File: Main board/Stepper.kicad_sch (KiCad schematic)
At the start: 10 parts, among them IC1 DRV8426RGER, J3 Conn_01x04

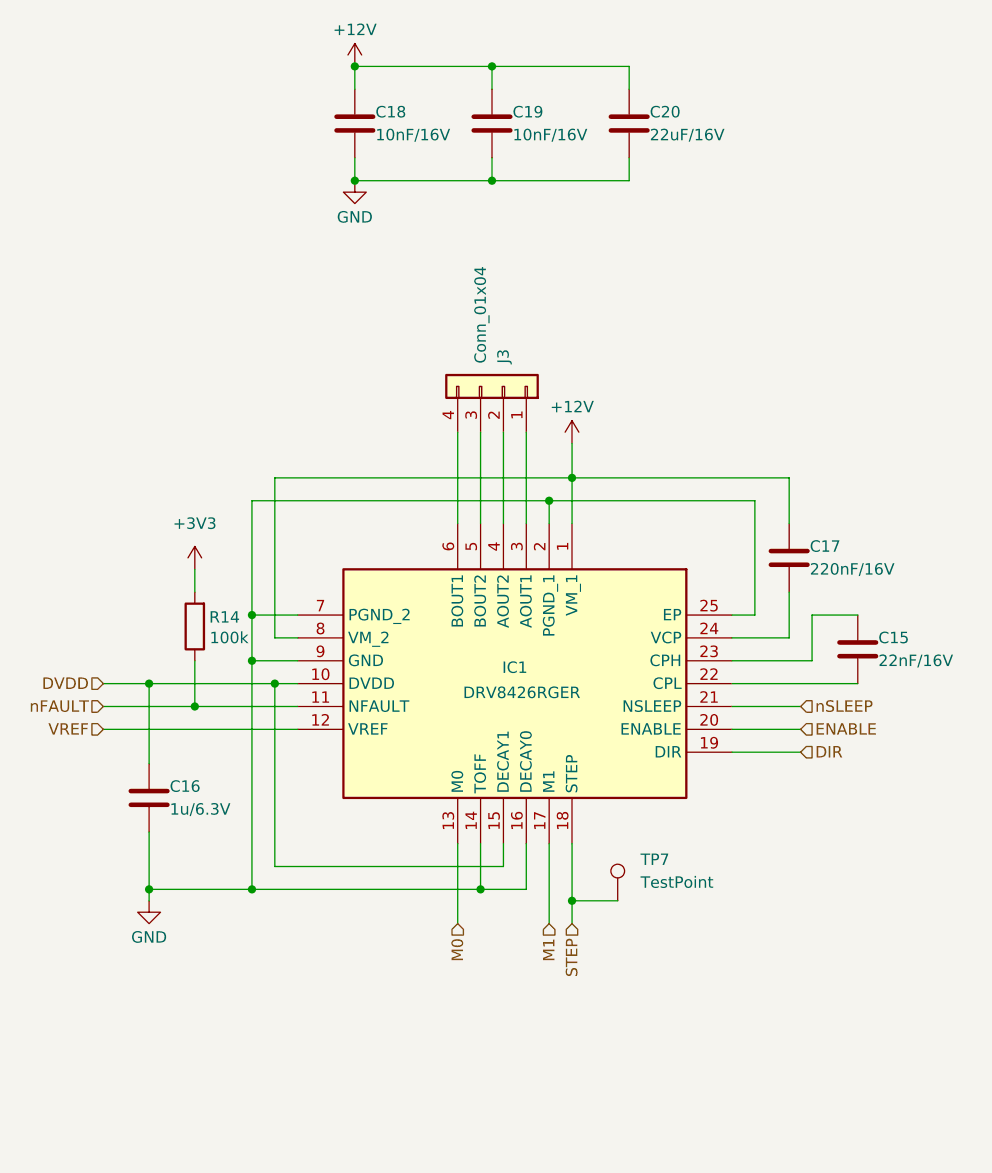
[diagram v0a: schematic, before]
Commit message: Main board updated to v0.3
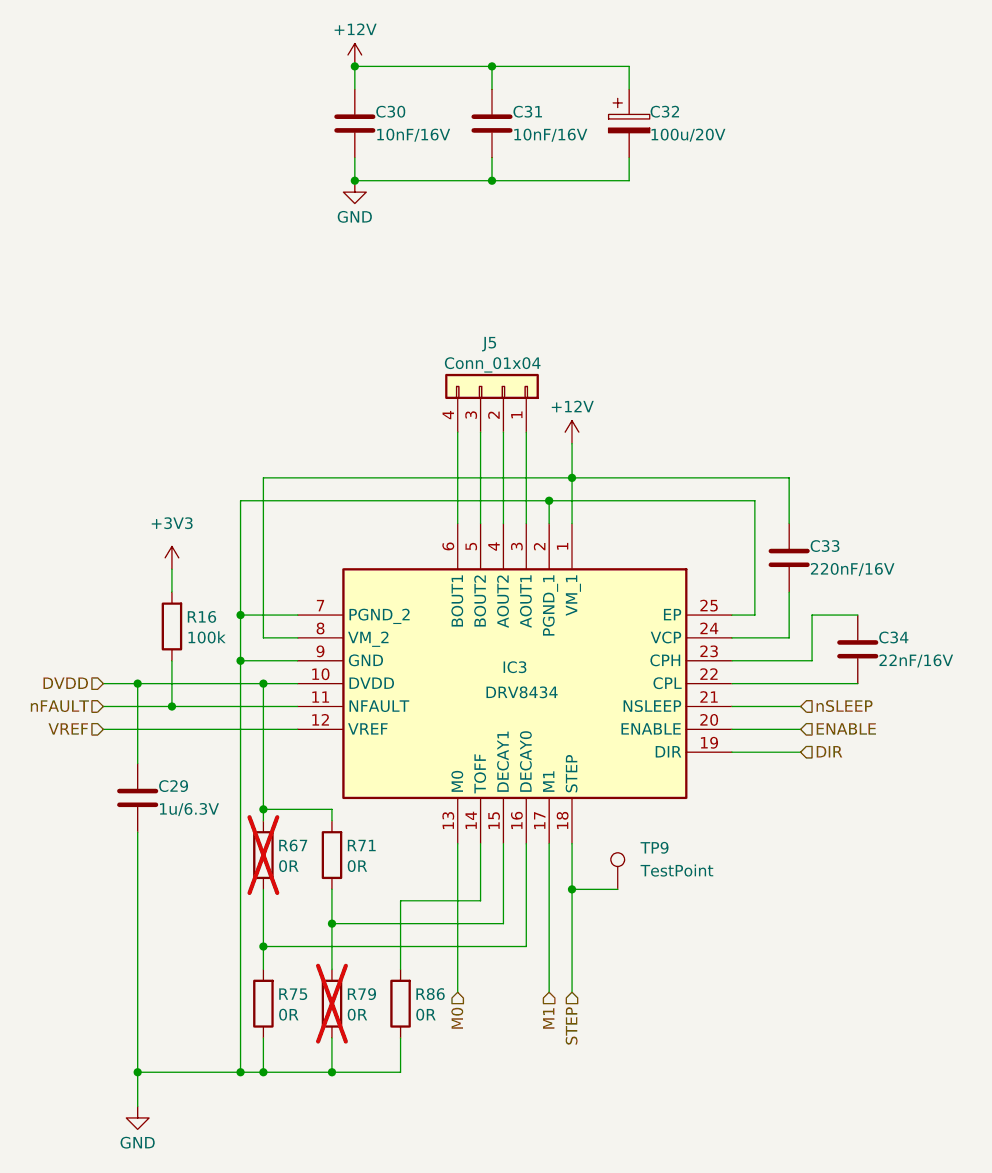
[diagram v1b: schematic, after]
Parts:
- added R67, R71, R75, R79, R86: 0R, Resistor_SMD:R_0402_1005Metric, symbol Device:R
- C32: renamed from C20; value 22uF/16V -> 100u/20V; footprint Capacitor_SMD:C_0805_2012Metric -> Capacitor_Tantalum_SMD:CP_EIA-7343-15_Kemet-W; symbol Device:C -> Device:C_Polarized
- IC3: renamed from IC1; value DRV8426RGER -> DRV8434
- renumbered C16 to C29, C18 to C30, C19 to C31, C17 to C33, C15 to C34, J3 to J5, R14 to R16, TP7 to TP9
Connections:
- net DVDD: now also R67.2, R71.2; no longer IC3.15 (DECAY1)
- net GND: now also R75.1, R79.1, R86.1; no longer IC3.14 (TOFF), IC3.16 (DECAY0)
- new net: IC3.15 (DECAY1), R71.1, R79.2
- new net: IC3.14 (TOFF), R86.2
- new net: IC3.16 (DECAY0), R67.1, R75.2
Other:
- moved on the sheet: C29, R16, TP9

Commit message: schema updated
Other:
- moved on the sheet: C30, C31, C32, J5

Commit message: Main board updated to v0.3
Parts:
- TP9: footprint TestPoint:TestPoint_Pad_D1.5mm -> TestPoint:TestPoint_Pad_D1.0mm
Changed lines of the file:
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@@
 			)
 		)
-		(property "Footprint" "TestPoint:TestPoint_Pad_D1.5mm"
+		(property "Footprint" "TestPoint:TestPoint_Pad_D1.0mm"
 			(at 170.18 133.35 0)
 			(effects

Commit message: Added part numbers for simpler ordering
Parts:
- C29: value 1u/6.3V -> 1uF; Part Number (none) -> GRM155Z71A105KE01J
- C30, C31: value 10nF/16V -> 10nF; Part Number (none) -> GRM155R71H103JA88D
- C32: Alternative PN (none) -> TAJD107K020RNJ; Part Number (none) -> 293D107X9020D2TE3
- C33: value 220nF/16V -> 220nF; Part Number (none) -> GCM155R71C224KE02J
- C34: value 22nF/16V -> 22nF; Part Number (none) -> GRM155R71E223JA61D
- IC3: value DRV8434 -> DRV8434/24; Alternative PN (none) -> DRV8424RGER; Manufacturer_Part_Number DRV8426RGER -> DRV8434RGER; Mouser Part Number 595-DRV8426RGER -> DRV8434RGER; Part Number (none) -> DRV8434RGER
- J5, TP9: now left out of the parts list
- R16: Part Number (none) -> CRCW0402100KFKEE
- R67, R71, R75, R79, R86: Part Number (none) -> CRCW04020000Z0EDC
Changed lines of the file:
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@@
 		(unit 1)
 		(exclude_from_sim no)
-		(in_bom yes)
+		(in_bom no)
 		(on_board yes)
 		(dnp no)
@@
 			)
 		)
-		(property "Value" "220nF/16V"
+		(property "Value" "220nF"
 			(at 186.436 97.79 0)
 			(effects
@@
 		(property "Description" "Unpolarized capacitor"
 			(at 184.15 96.52 0)
+			(effects
+				(font
+					(size 1.27 1.27)
+				)
+				(hide yes)
+			)
+		)
+		(property "Part Number" "GCM155R71C224KE02J"
+			(at 184.15 94.234 0)
 			(effects
 				(font
@@
 			)
 		)
+		(property "Part Number" "CRCW04020000Z0EDC"
+			(at 133.35 129.54 0)
+			(effects
+				(font
+					(size 1.27 1.27)
+				)
+				(hide yes)
+			)
+		)
 		(pin "2"
 		)
@@
 		(unit 1)
 		(exclude_from_sim no)
-		(in_bom yes)
+		(in_bom no)
 		(on_board yes)
 		(dnp no)
@@
 			)
 		)
-		(property "Value" "DRV8434"
+		(property "Value" "DRV8434/24"
 			(at 154.432 111.506 90)
 			(effects
@@
 			)
 		)
-		(property "Mouser Part Number" "595-DRV8426RGER"
+		(property "Mouser Part Number" "DRV8434RGER"
 			(at -324.74 124.46 0)
 			(effects
@@
 			)
 		)
-		(property "Manufacturer_Part_Number" "DRV8426RGER"
+		(property "Manufacturer_Part_Number" "DRV8434RGER"
 			(at -624.74 124.46 0)
 			(effects
@@
 				)
 				(justify left top)
+				(hide yes)
+			)
+		)
+		(property "Alternative PN" "DRV8424RGER"
+			(at 160.02 92.71 0)
+			(effects
+				(font
+					(size 1.27 1.27)
+				)
+				(hide yes)
+			)
+		)
+		(property "Part Number" "DRV8434RGER"
+			(at 160.02 92.71 0)
+			(effects
+				(font
+					(size 1.27 1.27)
+				)
 				(hide yes)
 			)
@@
 			)
 		)
-		(property "Value" "10nF/16V"
+		(property "Value" "10nF"
 			(at 138.176 62.23 0)
 			(effects
@@
 		(property "Description" "Unpolarized capacitor"
 			(at 135.89 60.96 0)
+			(effects
+				(font
+					(size 1.27 1.27)
+				)
+				(hide yes)
+			)
+		)
+		(property "Part Number" "GRM155R71H103JA88D"
+			(at 135.636 58.674 0)
 			(effects
 				(font
@@
 			)
 		)
-		(property "Value" "22nF/16V"
+		(property "Value" "22nF"
 			(at 194.056 107.95 0)
 			(effects
@@
 		(property "Description" "Unpolarized capacitor"
 			(at 191.77 106.68 0)
+			(effects
+				(font
+					(size 1.27 1.27)
+				)
+				(hide yes)
+			)
+		)
+		(property "Part Number" "GRM155R71E223JA61D"
+			(at 192.278 103.632 0)
 			(effects
 				(font
@@
 			)
 		)
+		(property "Part Number" "CRCW0402100KFKEE"
+			(at 115.57 104.14 0)
+			(effects
+				(font
+					(size 1.27 1.27)
+				)
+				(hide yes)
+			)
+		)
 		(pin "2"
 		)
@@
 			)
 		)
+		(property "Alternative PN" "TAJD107K020RNJ"
+			(at 166.37 60.96 0)
+			(effects
+				(font
+					(size 1.27 1.27)
+				)
+				(hide yes)
+			)
+		)
+		(property "Part Number" "293D107X9020D2TE3"
+			(at 166.37 60.96 0)
+			(effects
+				(font
+					(size 1.27 1.27)
+				)
+				(hide yes)
+			)
+		)
 		(pin "2"
 		)
@@
 			)
 		)
-		(property "Value" "1u/6.3V"
+		(property "Value" "1uF"
 			(at 114.046 124.46 0)
 			(effects
@@
 		)
 		(property "Description" "Unpolarized capacitor"
+			(at 111.76 123.19 0)
+			(effects
+				(font
+					(size 1.27 1.27)
+				)
+				(hide yes)
+			)
+		)
+		(property "Part Number" "GRM155Z71A105KE01J"
 			(at 111.76 123.19 0)
 			(effects
@@
 			)
 		)
+		(property "Part Number" "CRCW04020000Z0EDC"
+			(at 140.97 146.05 0)
+			(effects
+				(font
+					(size 1.27 1.27)
+				)
+				(hide yes)
+			)
+		)
 		(pin "2"
 		)
@@
 			)
 		)
-		(property "Value" "10nF/16V"
+		(property "Value" "10nF"
 			(at 153.416 62.23 0)
 			(effects
@@
 		(property "Description" "Unpolarized capacitor"
 			(at 151.13 60.96 0)
+			(effects
+				(font
+					(size 1.27 1.27)
+				)
+				(hide yes)
+			)
+		)
+		(property "Part Number" "GRM155R71H103JA88D"
+			(at 151.384 58.928 0)
 			(effects
 				(font
@@
 			)
 		)
+		(property "Part Number" "CRCW04020000Z0EDC"
+			(at 125.73 146.05 0)
+			(effects
+				(font
+					(size 1.27 1.27)
+				)
+				(hide yes)
+			)
+		)
 		(pin "2"
 		)
@@
 			)
 		)
+		(property "Part Number" "CRCW04020000Z0EDC"
+			(at 133.35 146.05 0)
+			(effects
+				(font
+					(size 1.27 1.27)
+				)
+				(hide yes)
+			)
+		)
 		(pin "2"
 		)
@@
 			(at 125.73 129.54 0)
 			(effects
+				(font
+					(size 1.27 1.27)
+				)
+				(hide yes)
+			)
+		)
+		(property "Part Number" "CRCW04020000Z0EDC"
+			(at 125.73 129.54 0)
+			(effects
